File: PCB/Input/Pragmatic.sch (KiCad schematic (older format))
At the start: 80 parts, among them J1 Conn_02x08_Odd_Even, J2 Conn_01x04, SW1 SW_Push, SW10 SW_Push, SW11 SW_Push, SW12 SW_Push, SW13 SW_Push, SW14 Q, SW15 W, SW16 E, SW17 R, SW18 T, SW19 SW_Push, SW2 SW_Push, SW20 A, SW21 S, SW22 D, SW23 F, SW24 G, SW25 SW_Push, SW26 Z, SW27 X, SW28 C, SW29 V, SW3 SW_Push, SW30 B, SW31 SW_Push, SW32 SW_Push, SW33 SW_Push, SW34 SW_Push, SW35 SW_Push, SW36 SW_Push, SW4 SW_Push, SW5 SW_Push, SW6 SW_Push, SW7 SW_Push, SW8 SW_Push, SW9 SW_Push

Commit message: tweaks
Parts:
- D1, D10, D11, D12, D13, D14, D15, D16, D17, D18, D19, D2, D20, D21, D22, D23, D24, D25, D26, D27, D28, D29, D3, D30, D31, D32, D33, D34, D35, D36, D4, D5, D6, D7, D8, D9: value D -> 1N4148
- D37: value LED -> Green LED 520nm
- H1, H2, H3, H4: footprint MountingHole:MountingHole_3.2mm_M3_DIN965_Pad_TopBottom -> MountingHole:MountingHole_3.2mm_M3
- J1: value Conn_02x08_Odd_Even -> 2X8P IDC Connector Header Pitch 2.54mm
- J2: value Conn_01x04 -> Expansion pins
- R1: value R -> 100Ω
- SW14: value Q -> SW_Push
- SW15: value W -> SW_Push
- SW16: value E -> SW_Push
- SW17: value R -> SW_Push
- SW18: value T -> SW_Push
- SW20: value A -> SW_Push
- SW21: value S -> SW_Push
- SW22: value D -> SW_Push
- SW23: value F -> SW_Push
- SW24: value G -> SW_Push
- SW26: value Z -> SW_Push
- SW27: value X -> SW_Push
- SW28: value C -> SW_Push
- SW29: value V -> SW_Push
- SW30: value B -> SW_Push
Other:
- moved on the sheet: H1, H2, H3, H4

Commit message: gerber
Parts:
- added H5: MountingHole, MountingHole:MountingHole_3.2mm_M3, symbol Mechanical:MountingHole
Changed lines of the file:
@@
 Text GLabel 5750 3150 0    50   Input ~ 0
 Col5
+$Comp
+L Mechanical:MountingHole H5
+U 1 1 6199E1A3
+P 10100 6200
+F 0 "H5" H 10200 6246 50  0000 L CNN
+F 1 "MountingHole" H 10200 6155 50  0000 L CNN
+F 2 "MountingHole:MountingHole_3.2mm_M3" H 10100 6200 50  0001 C CNN
+F 3 "~" H 10100 6200 50  0001 C CNN
+	1    10100 6200
+	1    0    0    -1
+$EndComp
 $EndSCHEMATC

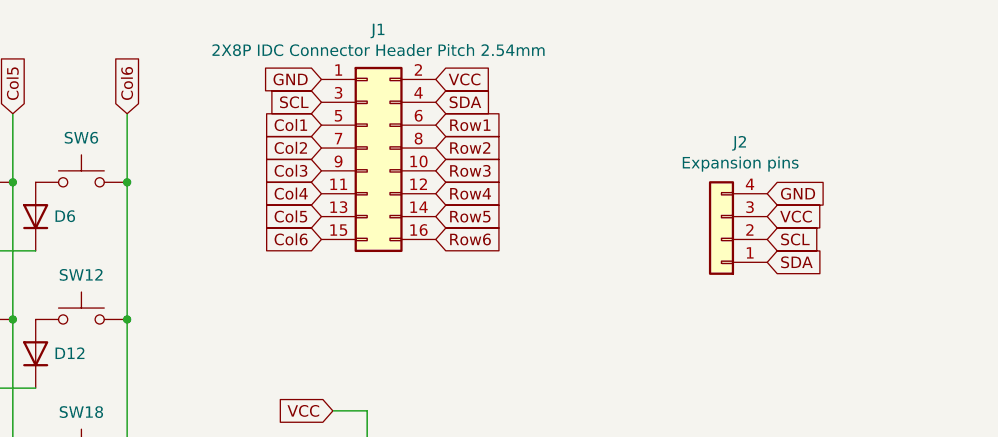
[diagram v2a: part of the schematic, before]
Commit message: 16P back to 14P, all via under pad
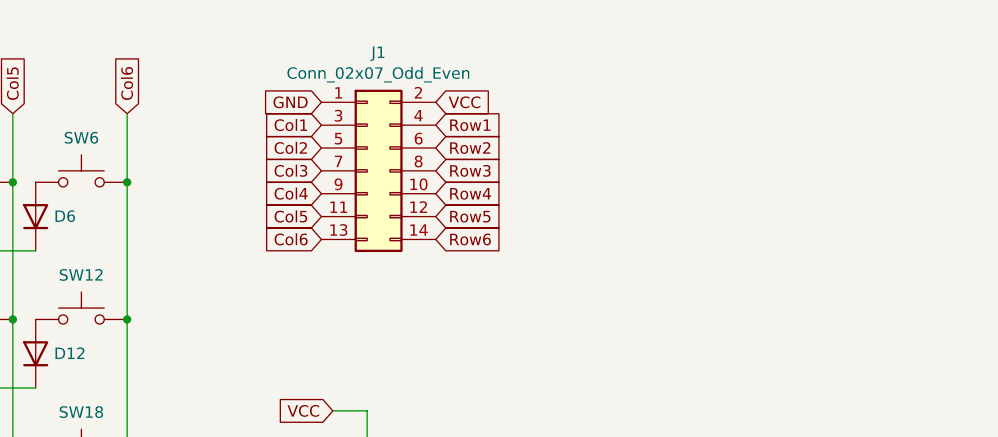
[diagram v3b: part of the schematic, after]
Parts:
- removed J1: 2X8P IDC Connector Header Pitch 2.54mm, Pragmatic:IDC-Header_2x08_P2.54mm_Vertical_Mirrored, symbol Connector_Generic:Conn_02x08_Odd_Even
- removed J2: Expansion pins, Connector_PinSocket_2.54mm:PinSocket_1x04_P2.54mm_Vertical, symbol Connector_Generic:Conn_01x04
- added J1: Conn_02x07_Odd_Even, Pragmatic:IDC-Header_2x07_P2.54mm_Vertical_Mirrored, symbol Connector_Generic:Conn_02x07_Odd_Even
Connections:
- net +5V: now also J1.2 (Pin_2)
- net Col1: now also J1.3 (Pin_3)
- net Col2: now also J1.5 (Pin_5)
- net Col3: now also J1.7 (Pin_7)
- net Col4: now also J1.9 (Pin_9)
- net Col5: now also J1.11 (Pin_11)
- net Col6: now also J1.13 (Pin_13)
- net GND: now also J1.1 (Pin_1)
- net Row1: now also J1.4 (Pin_4)
- net Row2: now also J1.6 (Pin_6)
- net Row3: now also J1.8 (Pin_8)
- net Row4: now also J1.10 (Pin_10)
- net Row5: now also J1.12 (Pin_12)
- net Row6: now also J1.14 (Pin_14)
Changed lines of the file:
@@
 	10550 4050 10150 4050
 Connection ~ 10150 4050
-Text GLabel 6250 2550 2    50   Input ~ 0
+Text GLabel 6250 2650 2    50   Input ~ 0
 VCC
-Text GLabel 5750 2550 0    50   Input ~ 0
+Text GLabel 5750 2650 0    50   Input ~ 0
 GND
-Text GLabel 6250 2650 2    50   Input ~ 0
-SDA
-Text GLabel 5750 2650 0    50   Input ~ 0
-SCL
 Text GLabel 6250 2750 2    50   Input ~ 0
 Row1
@@
 Text GLabel 5750 3250 0    50   Input ~ 0
 Col6
-Text GLabel 7700 3050 2    50   Input ~ 0
-GND
-Text GLabel 7700 3250 2    50   Input ~ 0
-SCL
-Text GLabel 7700 3350 2    50   Input ~ 0
-SDA
-Text GLabel 7700 3150 2    50   Input ~ 0
-VCC
-$Comp
-L Connector_Generic:Conn_01x04 J2
-U 1 1 6195FBC7
-P 7500 3250
-F 0 "J2" H 7418 2825 50  0000 C CNN
-F 1 "Expansion pins" H 7418 2916 50  0000 C CNN
-F 2 "Connector_PinSocket_2.54mm:PinSocket_1x04_P2.54mm_Vertical" H 7500 3250 50  0001 C CNN
-F 3 "~" H 7500 3250 50  0001 C CNN
-	1    7500 3250
-	-1   0    0    1
-$EndComp
 $Comp
 L Device:R R1
@@
 	1    0    0    -1
 $EndComp
-$Comp
-L Connector_Generic:Conn_02x08_Odd_Even J1
-U 1 1 6194905D
-P 5950 2850
-F 0 "J1" H 6000 3367 50  0000 C CNN
-F 1 "2X8P IDC Connector Header Pitch 2.54mm" H 6000 3276 50  0000 C CNN
-F 2 "Pragmatic:IDC-Header_2x08_P2.54mm_Vertical_Mirrored" H 5950 2850 50  0001 C CNN
-F 3 "https://datasheet.lcsc.com/lcsc/1811151542_BOOMELE-Boom-Precision-Elec-C3406_C3406.pdf" H 5950 2850 50  0001 C CNN
-F 4 "C3406" H 5950 2850 50  0001 C CNN "LCSC"
-	1    5950 2850
-	1    0    0    -1
-$EndComp
 Text GLabel 5750 2750 0    50   Input ~ 0
 Col1
@@
 	1    0    0    -1
 $EndComp
+$Comp
+L Connector_Generic:Conn_02x07_Odd_Even J1
+U 1 1 61AAACE1
+P 5950 2950
+F 0 "J1" H 6000 3467 50  0000 C CNN
+F 1 "Conn_02x07_Odd_Even" H 6000 3376 50  0000 C CNN
+F 2 "Pragmatic:IDC-Header_2x07_P2.54mm_Vertical_Mirrored" H 5950 2950 50  0001 C CNN
+F 3 "~" H 5950 2950 50  0001 C CNN
+	1    5950 2950
+	1    0    0    -1
+$EndComp

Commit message: build instruction draft
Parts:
- D37: value Green LED 520nm -> White LED; LCSC C2297 -> C434434
- J1: value Conn_02x07_Odd_Even -> Hand-Soldering; LCSC (none) -> C3406
- R1: value 100Ω -> 1.5K 1/8W; LCSC C17408 -> C4310
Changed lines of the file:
@@
 P 5950 4350
 F 0 "R1" H 6020 4396 50  0000 L CNN
-F 1 "100Ω" H 6020 4305 50  0000 L CNN
+F 1 "1.5K 1/8W" H 6020 4305 50  0000 L CNN
 F 2 "Pragmatic:R_0805_With_Shadow" V 5880 4350 50  0001 C CNN
-F 3 "https://datasheet.lcsc.com/lcsc/1809140113_UNI-ROYAL-Uniroyal-Elec-0402WGF1000TCE_C25076.pdf" H 5950 4350 50  0001 C CNN
-F 4 "C17408" H 5950 4350 50  0001 C CNN "LCSC"
+F 3 "https://datasheet.lcsc.com/lcsc/1810281220_UNI-ROYAL-Uniroyal-Elec-0805W8F1501T5E_C4310.pdf" H 5950 4350 50  0001 C CNN
+F 4 "C4310" H 5950 4350 50  0001 C CNN "LCSC"
 	1    5950 4350
 	1    0    0    -1
@@
 P 5950 4850
 F 0 "D37" V 5989 4732 50  0000 R CNN
-F 1 "Green LED 520nm" V 5898 4732 50  0000 R CNN
+F 1 "White LED" V 5898 4732 50  0000 R CNN
 F 2 "Pragmatic:LED_0805_With_Shadow" H 5950 4850 50  0001 C CNN
-F 3 "https://datasheet.lcsc.com/lcsc/1806151820_Hubei-KENTO-Elec-C2297_C2297.pdf" H 5950 4850 50  0001 C CNN
-F 4 "C2297" H 5950 4850 50  0001 C CNN "LCSC"
+F 3 "https://datasheet.lcsc.com/lcsc/1912111437_Yongyu-Photoelectric-SZYY0805W_C434434.pdf" H 5950 4850 50  0001 C CNN
+F 4 "C434434" H 5950 4850 50  0001 C CNN "LCSC"
 	1    5950 4850
 	0    -1   -1   0
@@
 P 5950 2950
 F 0 "J1" H 6000 3467 50  0000 C CNN
-F 1 "Conn_02x07_Odd_Even" H 6000 3376 50  0000 C CNN
+F 1 "Hand-Soldering" H 6000 3376 50  0000 C CNN
 F 2 "Pragmatic:IDC-Header_2x07_P2.54mm_Vertical_Mirrored" H 5950 2950 50  0001 C CNN
 F 3 "~" H 5950 2950 50  0001 C CNN
+F 4 "C3406" H 5950 2950 50  0001 C CNN "LCSC"
 	1    5950 2950
 	1    0    0    -1
